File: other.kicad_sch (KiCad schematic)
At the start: 0 parts

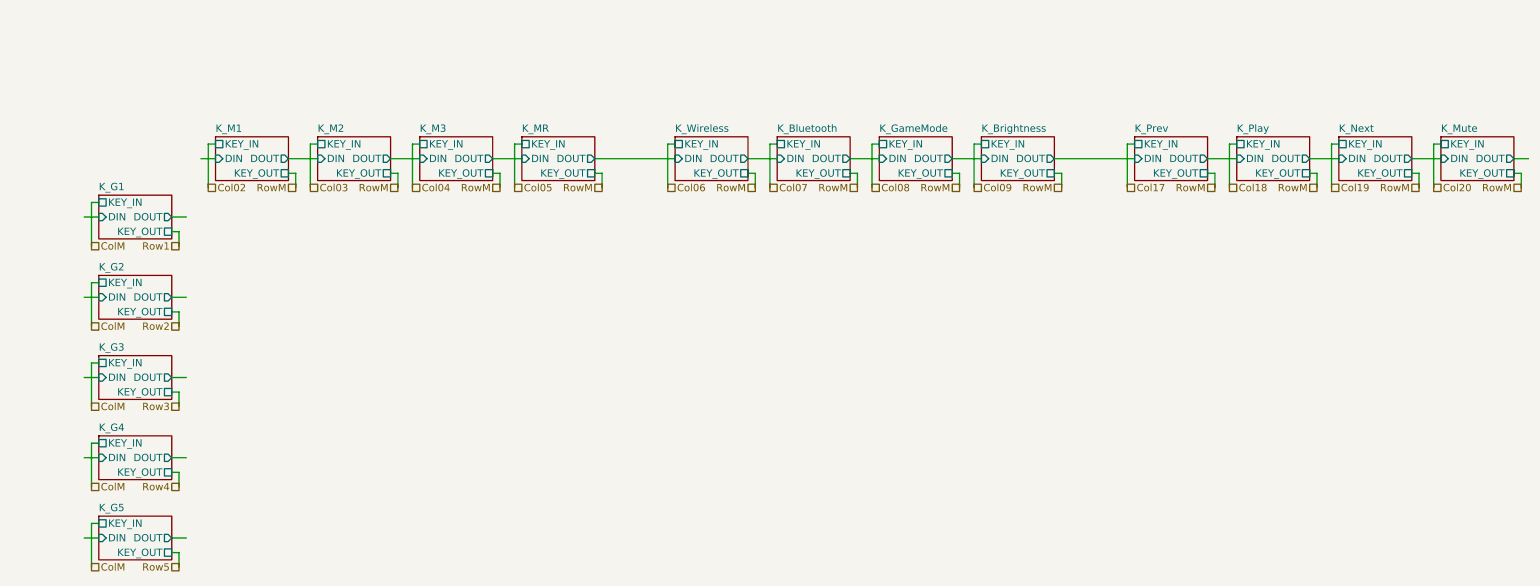
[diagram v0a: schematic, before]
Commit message: Unified key sch pages
One large page is simpler in this case
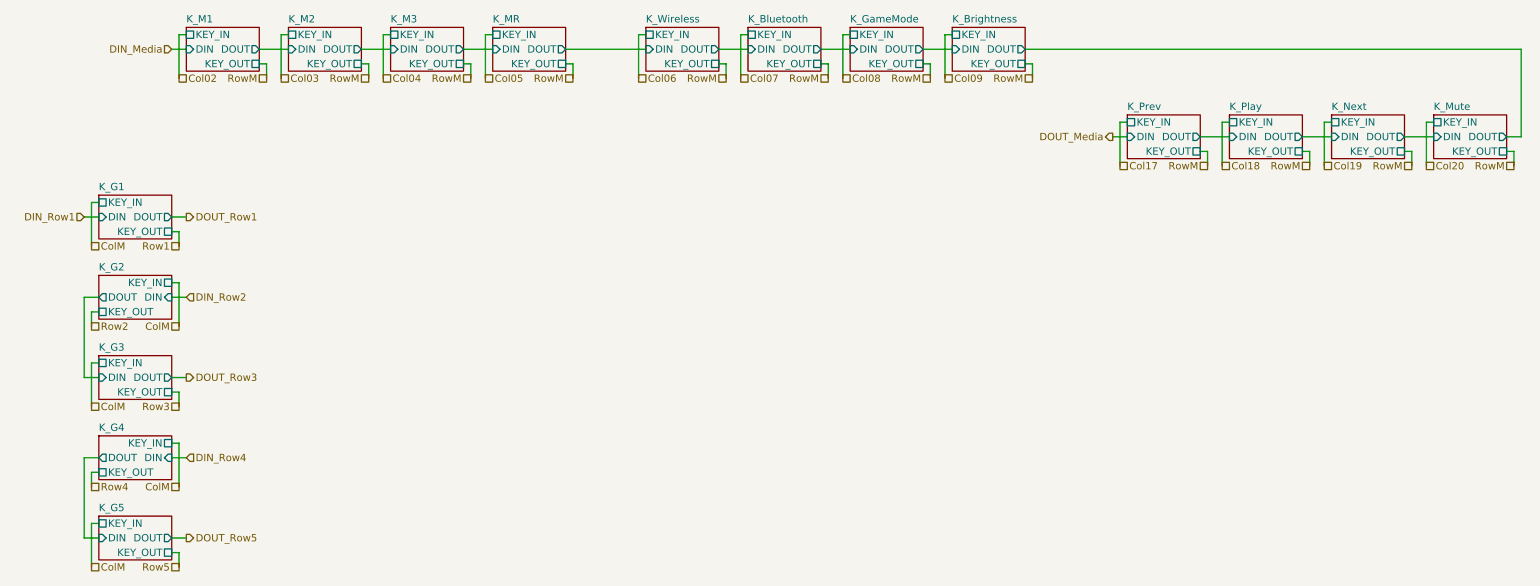
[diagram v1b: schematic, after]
